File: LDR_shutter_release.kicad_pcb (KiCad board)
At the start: 2 copper layers, 16 x 16 mm, 3 parts, among them J1 AudioJack4

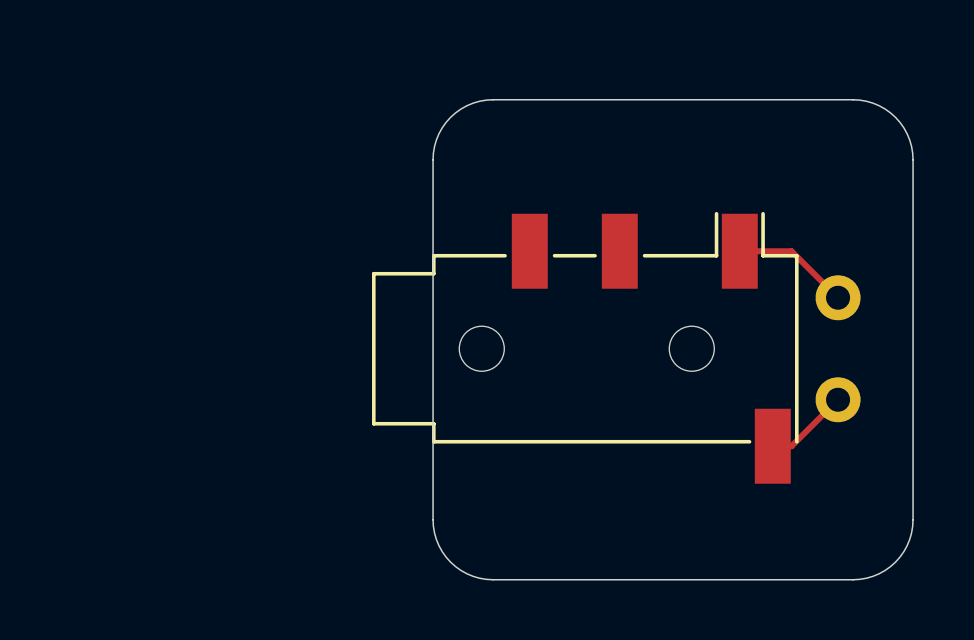
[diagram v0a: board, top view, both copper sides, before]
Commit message: Added footprint for second LDR, to allow full JLC PCBA of top-side
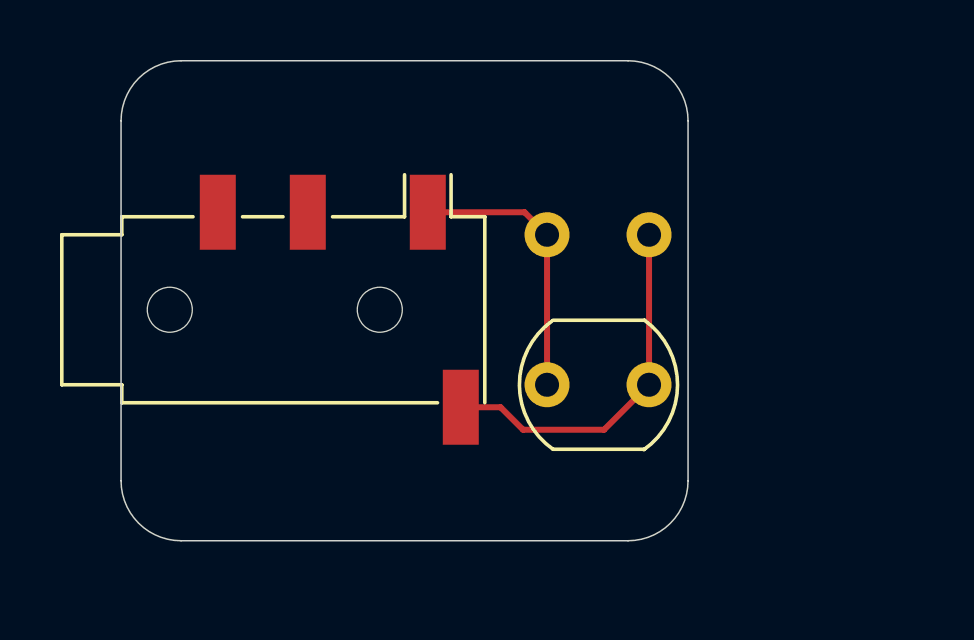
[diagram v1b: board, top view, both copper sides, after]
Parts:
- added R2: GL5528, OptoDevice:R_LDR_5.1x4.3mm_P3.4mm_Vertical, F.Cu at (131.2, 62.5)
- moved G*** 10.5 mm to (120.6, 55.7)
- moved J1 10.5 mm to (120.0, 60.0)
- moved R1 8.36 mm to (131.2, 57.5), turned to 180 degrees
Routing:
- net Net-(J1-PadS): track 2.82 -> 12.2 mm
- net Net-(J1-PadT): track 3.92 -> 9.29 mm
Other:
- board size 16 x 16 mm -> 18.9 x 16 mm
- board text added: "V0.0.0"
